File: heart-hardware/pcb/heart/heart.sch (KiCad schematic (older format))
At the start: 51 parts, among them J1 3V0, J2 DIO, J3 CLK, J4 GND, SW1 SW_SPDT, U1 STM32L031F6Px, U2 TCA6416APWR, U3 LIS3DH

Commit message: Update heart.sch
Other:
- note added: "check stm wakeup pins and connect to lis3dh interrupt lines\n"
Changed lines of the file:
@@
 	1    0    0    -1
 $EndComp
-Text Notes 1110 6640 0    197  ~ 39
+Text Notes 1730 -1190 0    197  ~ 39
 add decoupling capacitors!
 NoConn ~ 10000 3500
@@
 	-1   0    0    1
 $EndComp
-Text Notes 1140 6960 0    197  ~ 39
+Text Notes 1760 -870 0    197  ~ 39
 add test pads for current probe
+Text Notes 1720 -550 0    197  ~ 39
+check stm wakeup pins and connect to lis3dh interrupt lines\n
 $EndSCHEMATC

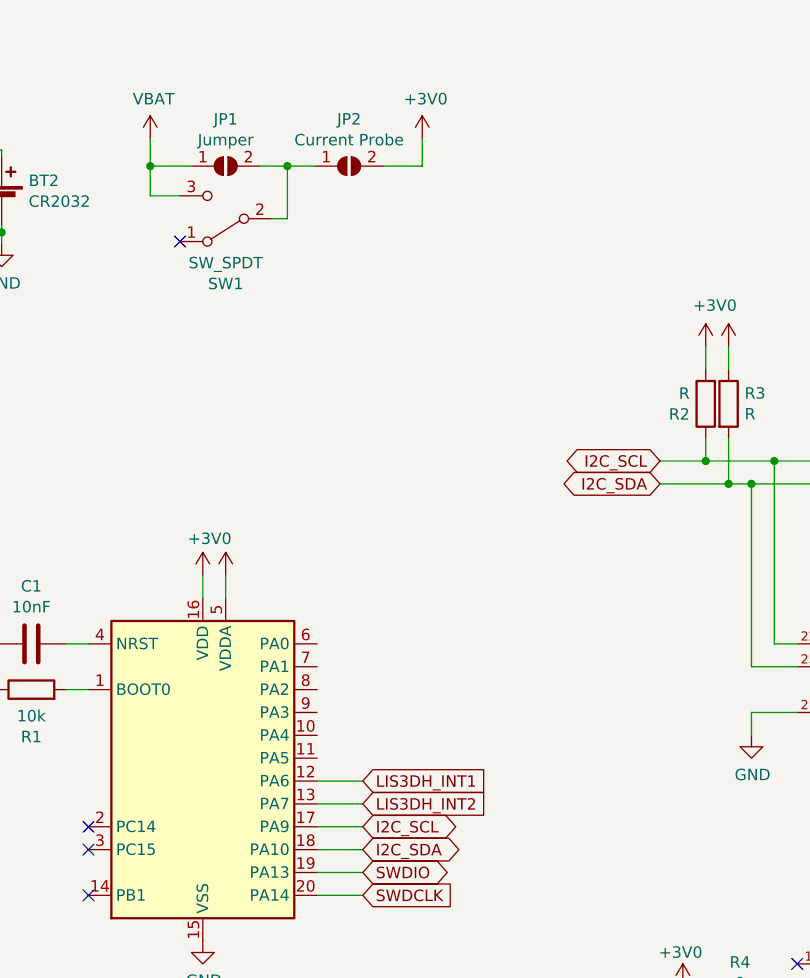
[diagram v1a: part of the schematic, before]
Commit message: Added current probe test points
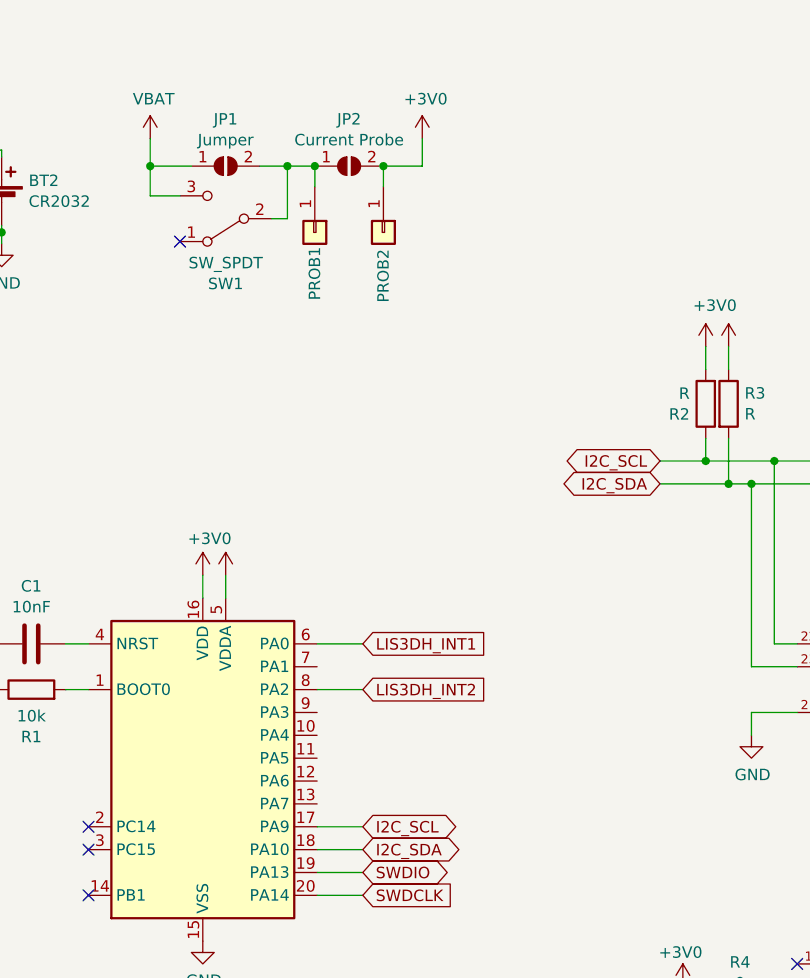
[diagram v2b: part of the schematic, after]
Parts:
- added J5: PROB1, TestPoint:TestPoint_Pad_2.5x2.5mm, symbol Connector_Generic:Conn_01x01
- added J6: PROB2, TestPoint:TestPoint_Pad_2.5x2.5mm, symbol Connector_Generic:Conn_01x01
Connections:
- net +3V0: now also J6.1 (Pin_1)
- net LIS3DH_INT1: now also U1.6 (PA0); no longer U1.12 (PA6)
- net LIS3DH_INT2: now also U1.8 (PA2); no longer U1.13 (PA7)
- net at JP1.2 (B), JP2.1 (A), SW1.2 (B): now also J5.1 (Pin_1)
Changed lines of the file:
@@
-$EndComp
-$Comp
-L MCU_ST_STM32L0:STM32L031F6Px U1
-U 1 1 61C303F2
-P 2300 3600
-F 0 "U1" H 2300 2510 50  0000 C CNN
-F 1 "STM32L031F6Px" H 2300 2420 50  0000 C CNN
-F 2 "Package_SO:TSSOP-20_4.4x6.5mm_P0.65mm" H 1900 2900 50  0001 R CNN
-F 3 "http://www.st.com/st-web-ui/static/active/en/resource/technical/document/datasheet/DM00140359.pdf" H 2300 3600 50  0001 C CNN
-	1    2300 3600
-	1    0    0    -1
 $EndComp
 $Comp
@@
 Wire Wire Line
 	2670 1010 2550 1010
-Wire Wire Line
-	2670 1010 2790 1010
 Connection ~ 2670 1010
 Wire Wire Line
@@
 Wire Wire Line
 	9000 3300 8600 3300
-Text GLabel 3000 3700 2    50   Input ~ 0
-LIS3DH_INT1
-Text GLabel 3000 3800 2    50   Input ~ 0
-LIS3DH_INT2
-Wire Wire Line
-	3000 3800 2800 3800
-Wire Wire Line
-	2800 3700 3000 3700
+Wire Wire Line
+	3000 3300 2800 3300
 Wire Wire Line
 	9400 2900 9400 2800
@@
 Text Notes 1720 -550 0    197  ~ 39
 check stm wakeup pins and connect to lis3dh interrupt lines\n
+Wire Wire Line
+	2800 3100 3000 3100
+Text GLabel 3000 3100 2    50   Input ~ 0
+LIS3DH_INT1
+$Comp
+L MCU_ST_STM32L0:STM32L031F6Px U1
+U 1 1 61C303F2
+P 2300 3600
+F 0 "U1" H 2300 2510 50  0000 C CNN
+F 1 "STM32L031F6Px" H 2300 2420 50  0000 C CNN
+F 2 "Package_SO:TSSOP-20_4.4x6.5mm_P0.65mm" H 1900 2900 50  0001 R CNN
+F 3 "http://www.st.com/st-web-ui/static/active/en/resource/technical/document/datasheet/DM00140359.pdf" H 2300 3600 50  0001 C CNN
+	1    2300 3600
+	1    0    0    -1
+$EndComp
+Text GLabel 3000 3300 2    50   Input ~ 0
+LIS3DH_INT2
+$Comp
+L Connector_Generic:Conn_01x01 J6
+U 1 1 61C4725D
+P 3090 1300
+F 0 "J6" H 3008 1075 50  0001 C CNN
+F 1 "PROB2" H 3280 1300 50  0000 C CNN
+F 2 "TestPoint:TestPoint_Pad_2.5x2.5mm" H 3090 1300 50  0001 C CNN
+F 3 "~" H 3090 1300 50  0001 C CNN
+	1    3090 1300
+	0    1    1    0
+$EndComp
+Wire Wire Line
+	2670 1010 2790 1010
+$Comp
+L Connector_Generic:Conn_01x01 J5
+U 1 1 61C62082
+P 2790 1300
+F 0 "J5" H 2708 1075 50  0001 C CNN
+F 1 "PROB1" H 2970 1300 50  0000 C CNN
+F 2 "TestPoint:TestPoint_Pad_2.5x2.5mm" H 2790 1300 50  0001 C CNN
+F 3 "~" H 2790 1300 50  0001 C CNN
+	1    2790 1300
+	0    1    1    0
+$EndComp
+Wire Wire Line
+	2790 1100 2790 1010
+Connection ~ 2790 1010
+Wire Wire Line
+	3090 1100 3090 1010
+Connection ~ 3090 1010
 $EndSCHEMATC

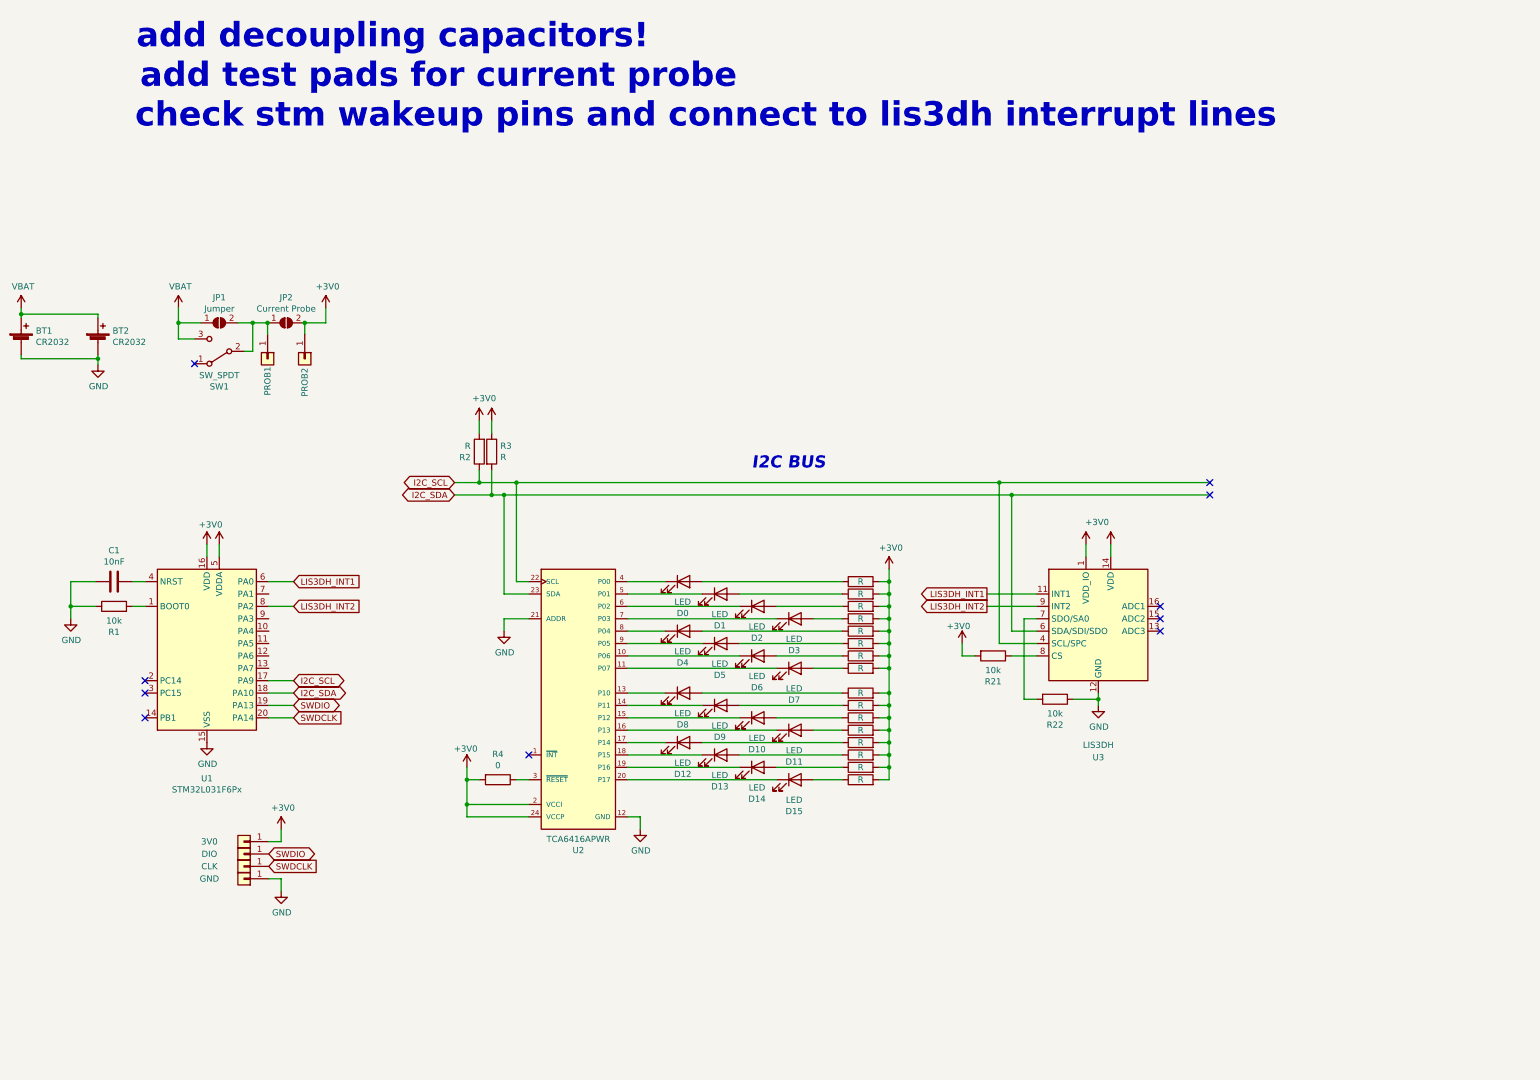
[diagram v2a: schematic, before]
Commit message: Added decoupling capacitors
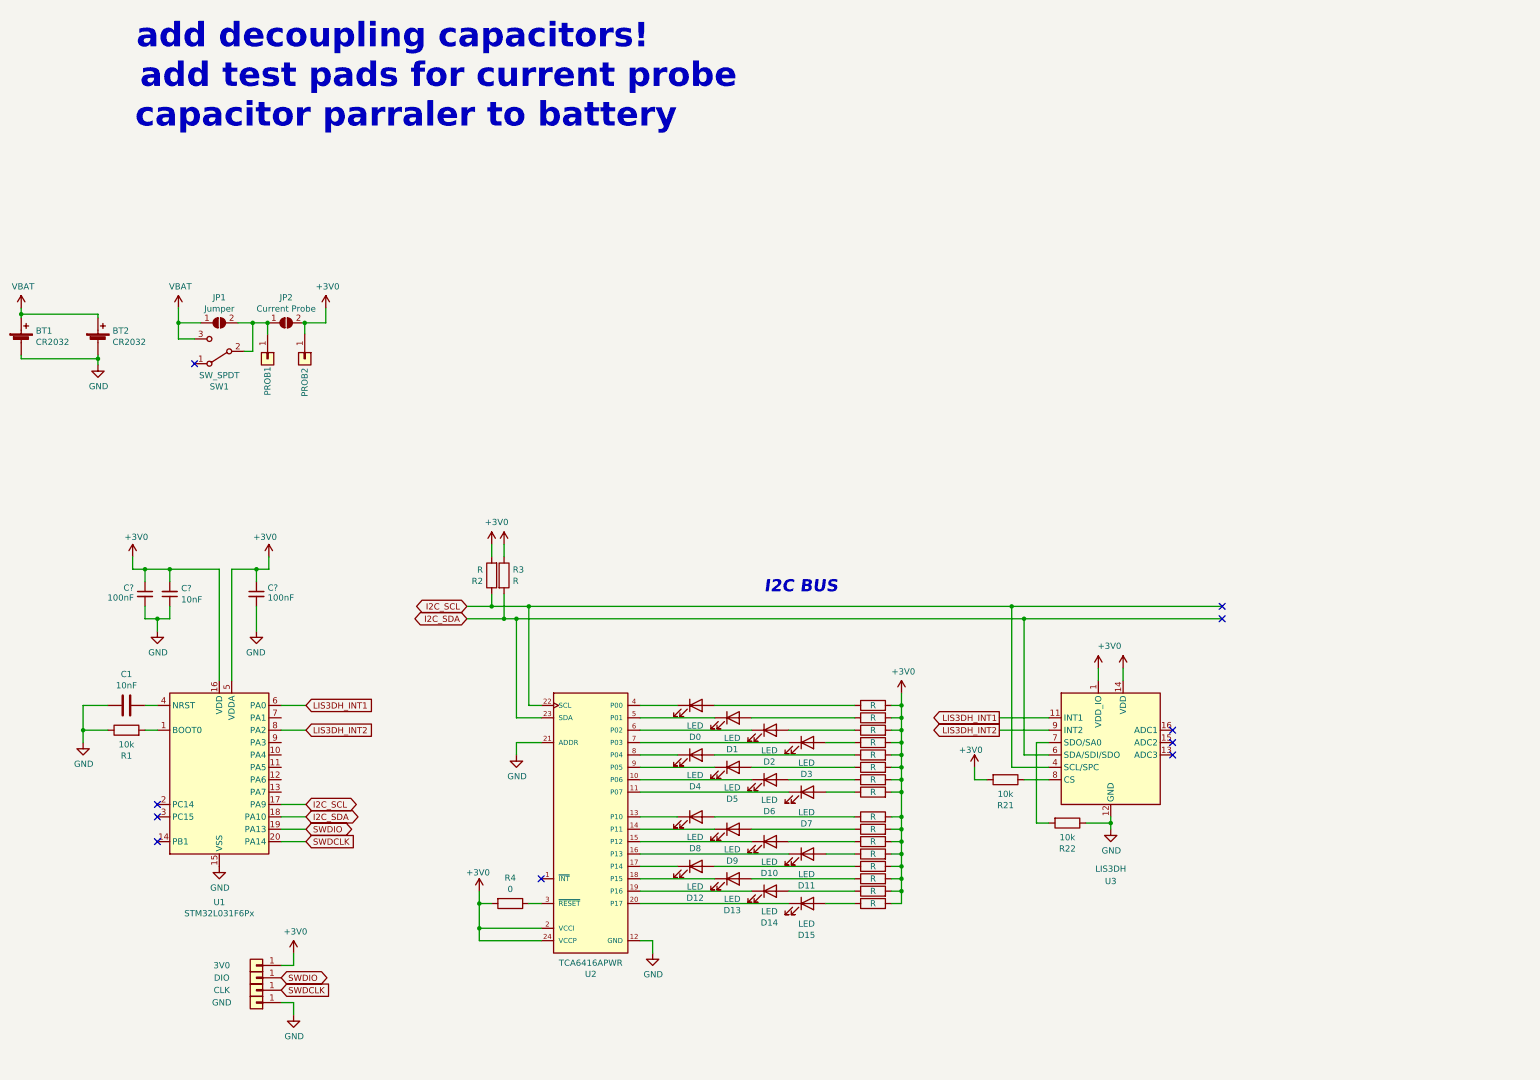
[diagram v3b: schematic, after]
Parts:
- added C? (x2): 100nF, symbol Device:C_Small
- added C?: 10nF, symbol Device:C_Small
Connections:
- net +3V0: now also C?.1, C?.1, C?.2
- net GND: now also C?.1, C?.2, C?.2
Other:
- note added: "capacitor parraler to battery\n"
- note removed: "check stm wakeup pins and connect to lis3dh interrupt lines\n"
- moved on the sheet: C1, D0, D1, D10, D11, D12, D13, D14, D15, D2, D3, D4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

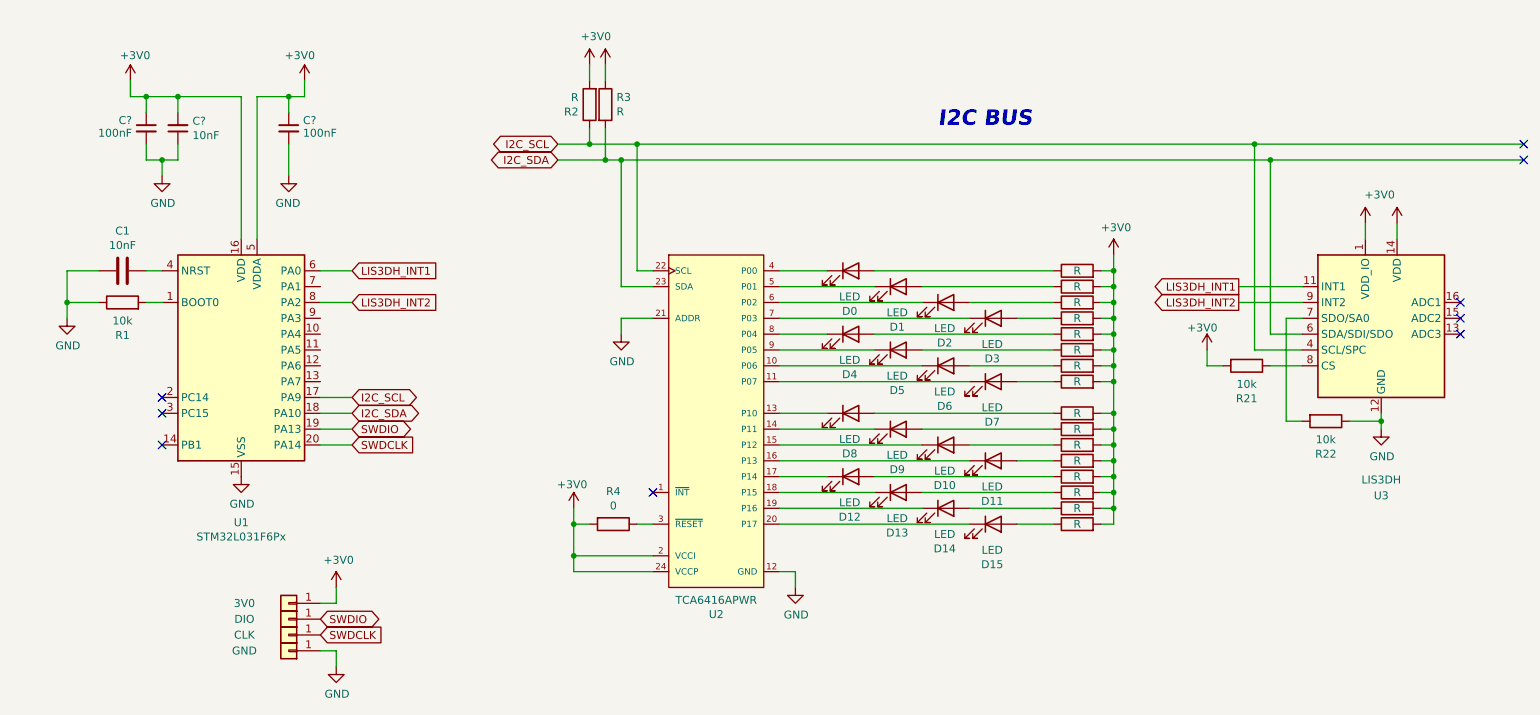
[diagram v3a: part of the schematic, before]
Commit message: Schematic complete (ver. 1.0), starting work on a pcb and choose footprints
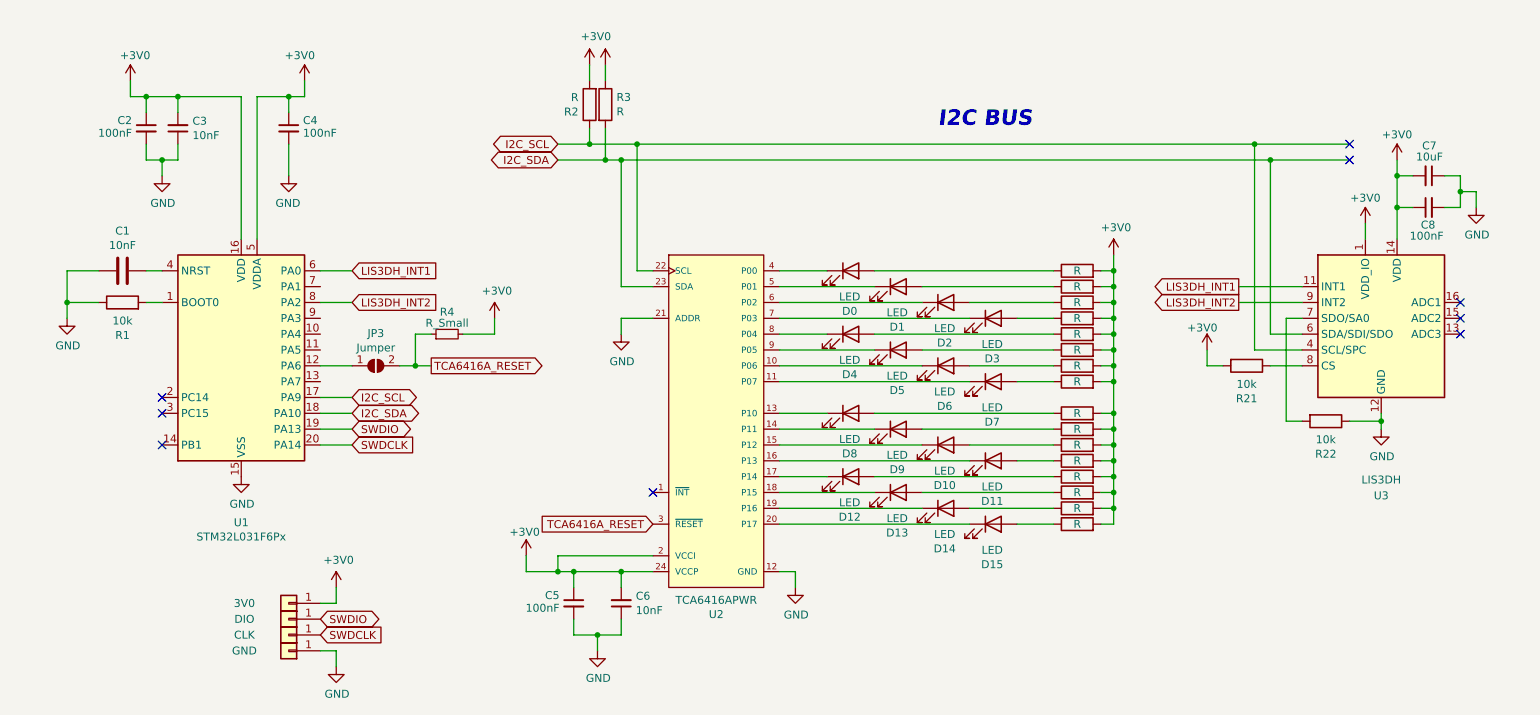
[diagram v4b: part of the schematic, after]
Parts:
- removed R4: 0, Capacitor_SMD:C_0603_1608Metric, symbol Device:R
- added C5, C8: 100nF, Capacitor_SMD:C_0603_1608Metric, symbol Device:C_Small
- added C6: 10nF, Capacitor_SMD:C_0603_1608Metric, symbol Device:C_Small
- added C7: 10uF, Capacitor_SMD:C_0603_1608Metric, symbol Device:C_Small
- added JP3: Jumper, Jumper:SolderJumper-2_P1.3mm_Open_RoundedPad1.0x1.5mm, symbol Jumper:SolderJumper_2_Open
- added R4: R_Small, Resistor_SMD:R_0603_1608Metric, symbol Device:R_Small
- C2, C3, C4: renamed from C?; footprint (none) -> Capacitor_SMD:C_0603_1608Metric
- R1, R2, R21, R22, R3: footprint Capacitor_SMD:C_0603_1608Metric -> Resistor_SMD:R_0603_1608Metric
- R10, R11, R12, R13, R14, R15, R16, R17, R18, R19, R20, R5, R6, R7, R8, R9: footprint Capacitor_SMD:C_0201_0603Metric -> Resistor_SMD:R_0603_1608Metric
- SW1: footprint Button_Switch_THT:SW_Tactile_SPST_Angled_PTS645Vx39-2LFS -> Button_Switch_SMD:SW_SPDT_PCM12
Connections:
- net +3V0: now also C5.1, C6.2, C7.2, C8.1, R4.2
- net GND: now also C5.2, C6.1, C7.1, C8.2
- net at U1.12 (PA6): now also JP3.1 (A)
- net TCA6416A_RESET: now reaches U2.3 (~RESET~)
- net TCA6416A_RESET: now also JP3.2 (B), R4.1

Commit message: PCB design update
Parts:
- removed J5: PROB1, TestPoint:TestPoint_Pad_2.5x2.5mm, symbol Connector_Generic:Conn_01x01
- removed J6: PROB2, TestPoint:TestPoint_Pad_2.5x2.5mm, symbol Connector_Generic:Conn_01x01
- added C0: 47uF, Capacitor_SMD:C_1210_3225Metric_Pad1.33x2.70mm_HandSolder, symbol Device:C_Small
- added C1: 100nF, Capacitor_SMD:C_0603_1608Metric, symbol Device:C_Small
- C2, C3, C4: footprint Capacitor_SMD:C_0603_1608Metric -> Capacitor_SMD:C_0402_1005Metric
- C5: renamed from C1; footprint Capacitor_SMD:C_0603_1608Metric -> Capacitor_SMD:C_0402_1005Metric
- C6: renamed from C5; footprint Capacitor_SMD:C_0603_1608Metric -> Capacitor_SMD:C_0402_1005Metric
- C7: renamed from C6; footprint Capacitor_SMD:C_0603_1608Metric -> Capacitor_SMD:C_0402_1005Metric
- C8: renamed from C7; footprint Capacitor_SMD:C_0603_1608Metric -> Capacitor_SMD:C_0402_1005Metric
- C9: renamed from C8; footprint Capacitor_SMD:C_0603_1608Metric -> Capacitor_SMD:C_0402_1005Metric
- D0, D1, D10, D11, D12, D13, D14, D15, D2, D3, D4, D5, D6, D7, D8, D9: footprint LED_THT:LED_D3.0mm -> LED_SMD:LED_0603_1608Metric
- J1, J2, J3, J4: footprint TestPoint:TestPoint_Pad_2.5x2.5mm -> TestPoint:TestPoint_Pad_1.0x1.0mm
- JP1: value Jumper -> PWR
- JP2: value Current Probe -> AMP
- R1, R10, R11, R12, R13, R14, R15, R16, R17, R18, R19, R20, R21, R22, R4, R5, R6, R7, R8, R9: footprint Resistor_SMD:R_0603_1608Metric -> Resistor_SMD:R_0402_1005Metric
- R2, R3: value R -> 10k; footprint Resistor_SMD:R_0603_1608Metric -> Resistor_SMD:R_0402_1005Metric
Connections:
- net +3V0: now also C0.1, C1.1
- net GND: now also C0.2, C1.2
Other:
- note removed: "add decoupling capacitors!"
- note removed: "add test pads for current probe"
- note removed: "capacitor parraler to battery\n"
- moved on the sheet: BT1, BT2, JP1, JP2, SW1
